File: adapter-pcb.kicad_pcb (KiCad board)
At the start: 2 copper layers, 90.2 x 95.9 mm, 53 parts, among them J1 SS5-80-3.50-L-D-K-TR, J2 DM3BT-DSF-PEJS, J3 Conn_02x05_Odd_Even, Q1 2N7002KQ-7, Q2 2N7002KQ-7, U1 TXS0102QDCURQ1, U2 LTC4300A-1IMS8_PBF, U3 TXS02612RTWR, U4 TPS79933QDDCRQ1

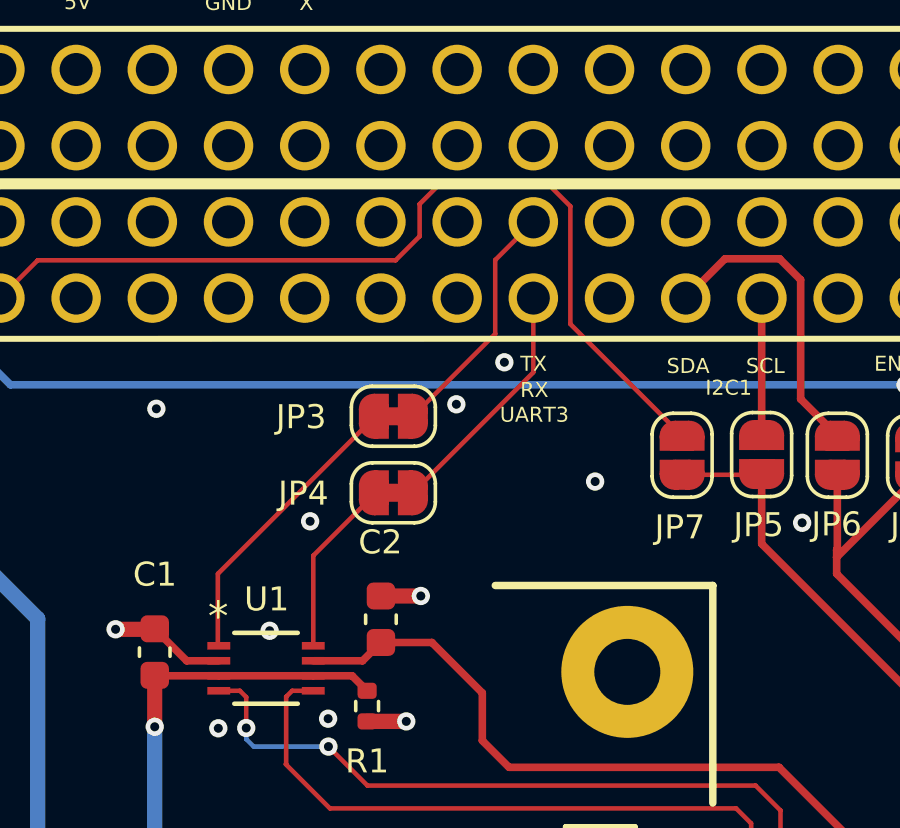
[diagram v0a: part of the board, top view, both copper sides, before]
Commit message: Reversed RX and TX pins to accommodate altered UART standard
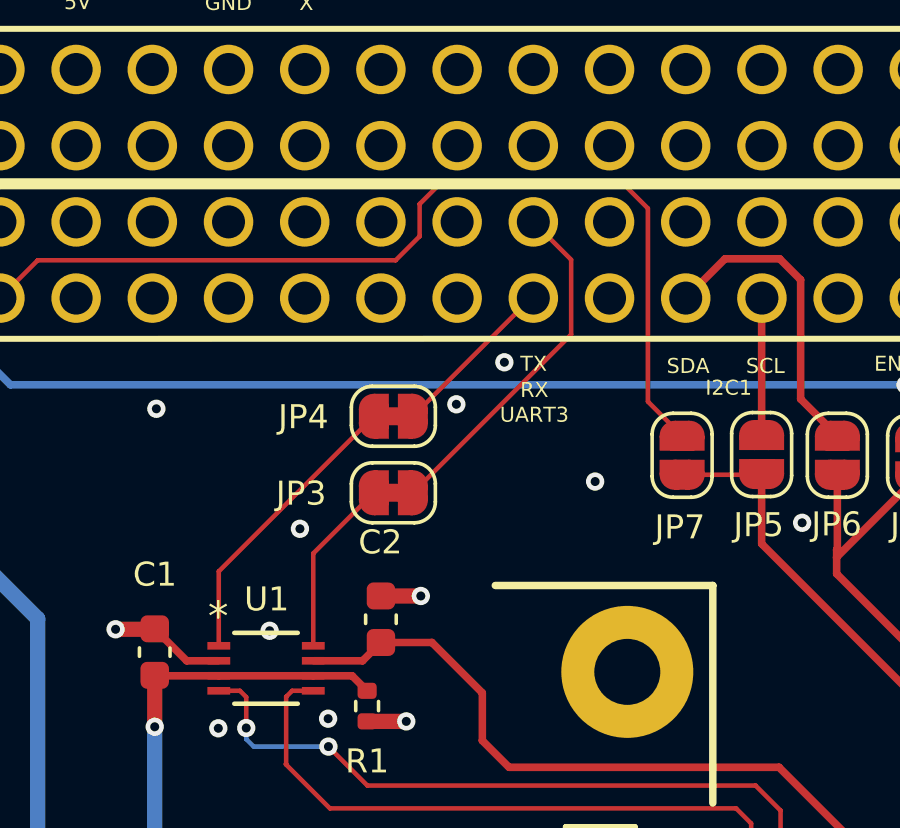
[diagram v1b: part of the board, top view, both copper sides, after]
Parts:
- moved JP3 2.55 mm to (160.4, 65.7)
- moved JP4 2.55 mm to (160.4, 63.1)
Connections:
- JP3 pad 1: /CSKB/UART-TXD LS -> /CSKB/UART-RXD LS
- JP4 pad 2: /CSKB/UART-RXD LS -> /CSKB/UART-TXD LS
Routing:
- net Net-(H1-Pin_38): track 8.54 -> 12.1 mm
- net Net-(H1-Pin_37): track 8.15 -> 5.65 mm
- net Net-(H1-Pin_23): track 30.8 -> 32.2 mm
